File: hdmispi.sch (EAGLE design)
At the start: 3 parts

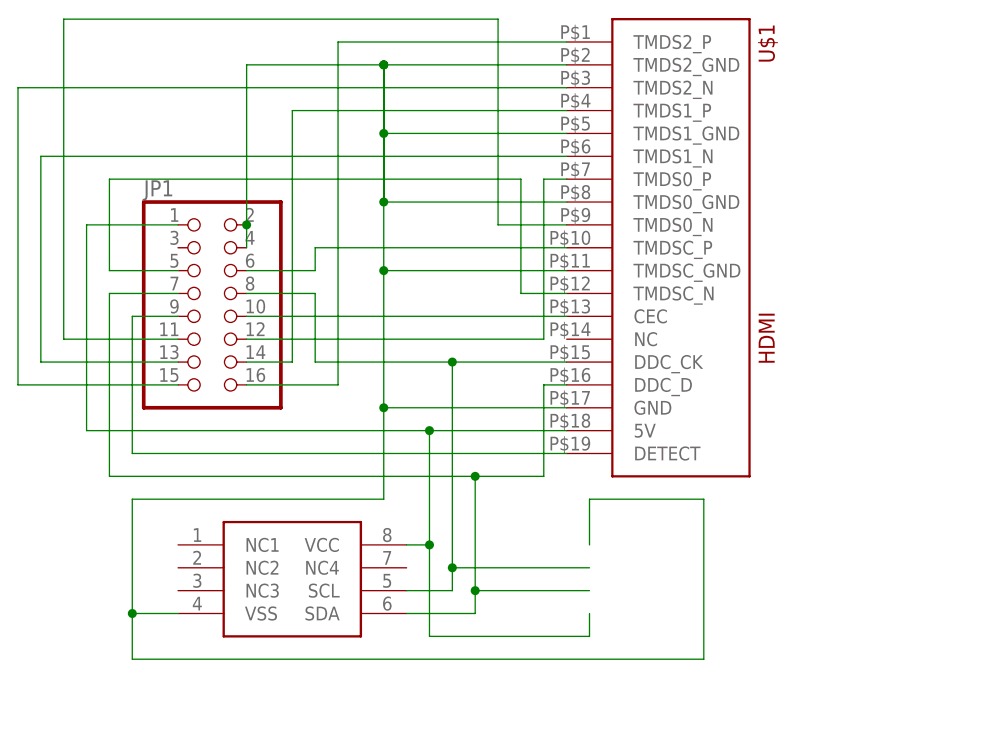
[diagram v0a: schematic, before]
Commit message: next rev of files, v1.0. Switched SDA/SCL wires by accident, doesn't work.
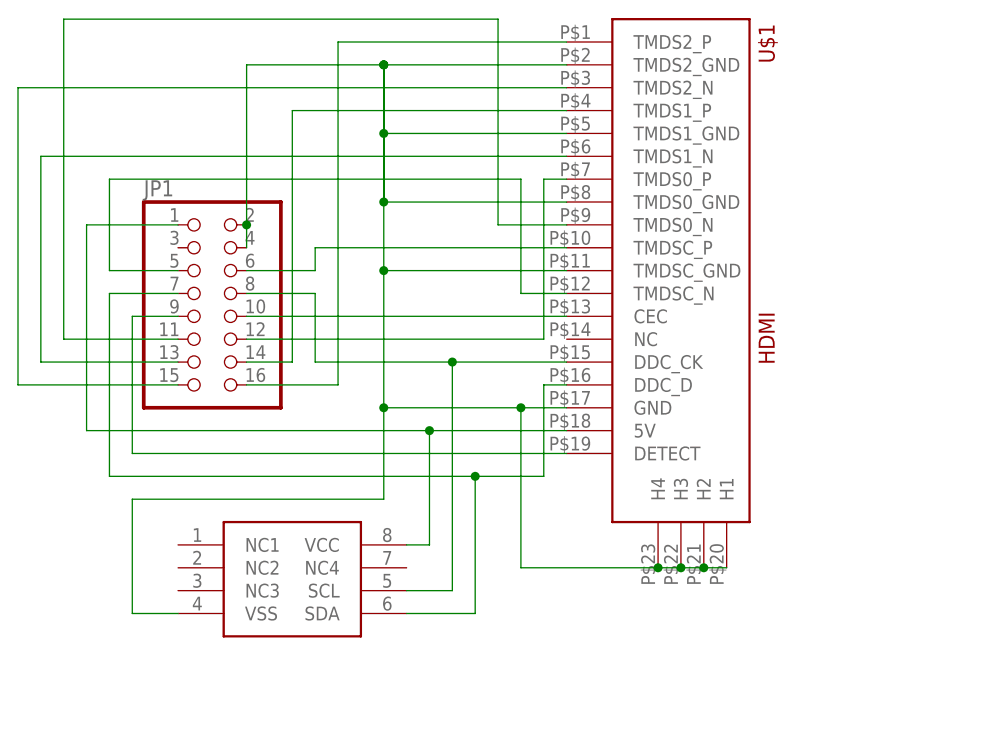
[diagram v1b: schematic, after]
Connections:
- net GND: now also U$1.H1, U$1.H2, U$1.H3, U$1.H4
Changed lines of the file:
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@@
 <wire x1="38.1" y1="83.82" x2="38.1" y2="96.52" width="0.1524" layer="91"/>
 <junction x="38.1" y="96.52"/>
-<wire x1="38.1" y1="83.82" x2="38.1" y2="73.66" width="0.1524" layer="91"/>
-<wire x1="38.1" y1="73.66" x2="55.88" y2="73.66" width="0.1524" layer="91"/>
-<wire x1="55.88" y1="73.66" x2="55.88" y2="76.2" width="0.1524" layer="91"/>
-<junction x="38.1" y="83.82"/>
 </segment>
 </net>
@@
 <pinref part="U$1" gate="G$1" pin="GND"/>
 <wire x1="33.02" y1="114.3" x2="33.02" y2="99.06" width="0.1524" layer="91"/>
-<wire x1="33.02" y1="99.06" x2="53.34" y2="99.06" width="0.1524" layer="91"/>
+<wire x1="33.02" y1="99.06" x2="48.26" y2="99.06" width="0.1524" layer="91"/>
 <junction x="33.02" y="129.54"/>
 <junction x="33.02" y="121.92"/>
@@
 <junction x="33.02" y="137.16"/>
 <pinref part="U$1" gate="G$1" pin="TMDSC_GND"/>
+<wire x1="48.26" y1="99.06" x2="53.34" y2="99.06" width="0.1524" layer="91"/>
 <wire x1="53.34" y1="114.3" x2="33.02" y2="114.3" width="0.1524" layer="91"/>
 <junction x="33.02" y="114.3"/>
@@
 <wire x1="33.02" y1="88.9" x2="33.02" y2="99.06" width="0.1524" layer="91"/>
 <junction x="33.02" y="99.06"/>
-<wire x1="55.88" y1="83.82" x2="55.88" y2="88.9" width="0.1524" layer="91"/>
-<wire x1="55.88" y1="88.9" x2="68.58" y2="88.9" width="0.1524" layer="91"/>
-<wire x1="68.58" y1="88.9" x2="68.58" y2="71.12" width="0.1524" layer="91"/>
-<wire x1="68.58" y1="71.12" x2="5.08" y2="71.12" width="0.1524" layer="91"/>
-<wire x1="5.08" y1="71.12" x2="5.08" y2="76.2" width="0.1524" layer="91"/>
-<junction x="5.08" y="76.2"/>
+<junction x="48.26" y="99.06"/>
+<wire x1="48.26" y1="99.06" x2="48.26" y2="81.28" width="0.1524" layer="91"/>
+<pinref part="U$1" gate="G$1" pin="H4"/>
+<junction x="63.5" y="81.28"/>
+<wire x1="48.26" y1="81.28" x2="63.5" y2="81.28" width="0.1524" layer="91"/>
+<pinref part="U$1" gate="G$1" pin="H3"/>
+<junction x="66.04" y="81.28"/>
+<wire x1="63.5" y1="81.28" x2="66.04" y2="81.28" width="0.1524" layer="91"/>
+<pinref part="U$1" gate="G$1" pin="H2"/>
+<junction x="68.58" y="81.28"/>
+<wire x1="66.04" y1="81.28" x2="68.58" y2="81.28" width="0.1524" layer="91"/>
+<pinref part="U$1" gate="G$1" pin="H1"/>
+<wire x1="68.58" y1="81.28" x2="71.12" y2="81.28" width="0.1524" layer="91"/>
 </segment>
 </net>
@@
 <pinref part="U$2" gate="G$1" pin="SDA"/>
 <wire x1="35.56" y1="76.2" x2="43.18" y2="76.2" width="0.1524" layer="91"/>
-<wire x1="43.18" y1="76.2" x2="43.18" y2="78.74" width="0.1524" layer="91"/>
 <junction x="43.18" y="91.44"/>
-<wire x1="43.18" y1="78.74" x2="43.18" y2="91.44" width="0.1524" layer="91"/>
-<wire x1="43.18" y1="78.74" x2="55.88" y2="78.74" width="0.1524" layer="91"/>
-<junction x="43.18" y="78.74"/>
+<wire x1="43.18" y1="76.2" x2="43.18" y2="91.44" width="0.1524" layer="91"/>
 </segment>
 </net>
@@
 <pinref part="U$2" gate="G$1" pin="SCL"/>
 <wire x1="35.56" y1="78.74" x2="40.64" y2="78.74" width="0.1524" layer="91"/>
-<wire x1="40.64" y1="78.74" x2="40.64" y2="81.28" width="0.1524" layer="91"/>
 <junction x="40.64" y="104.14"/>
-<wire x1="40.64" y1="81.28" x2="40.64" y2="104.14" width="0.1524" layer="91"/>
-<wire x1="40.64" y1="81.28" x2="55.88" y2="81.28" width="0.1524" layer="91"/>
-<junction x="40.64" y="81.28"/>
+<wire x1="40.64" y1="78.74" x2="40.64" y2="104.14" width="0.1524" layer="91"/>
 </segment>
 </net>

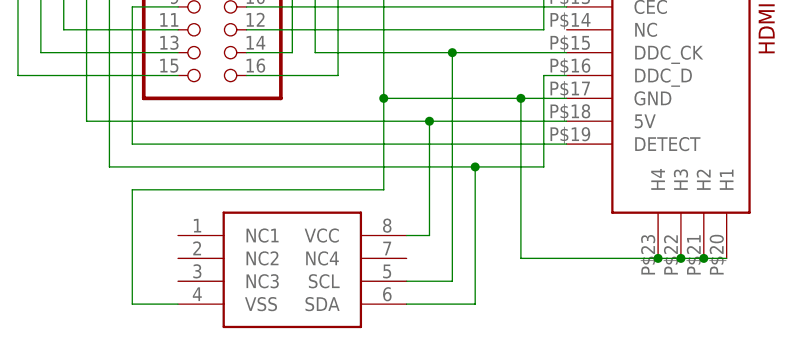
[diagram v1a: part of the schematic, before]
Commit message: fixed board and schematic with sda/scl corrected.
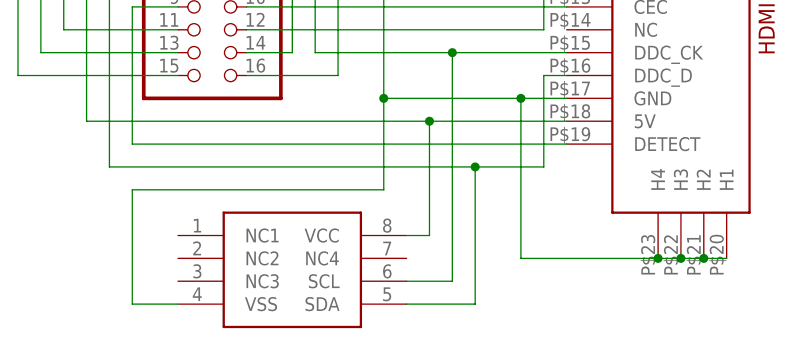
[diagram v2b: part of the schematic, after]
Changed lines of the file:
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@@
 <?xml version="1.0" encoding="utf-8"?>
 <!DOCTYPE eagle SYSTEM "eagle.dtd">
-<eagle version="7.2.0">
+<eagle version="7.6.0">
 <drawing>
 <settings>

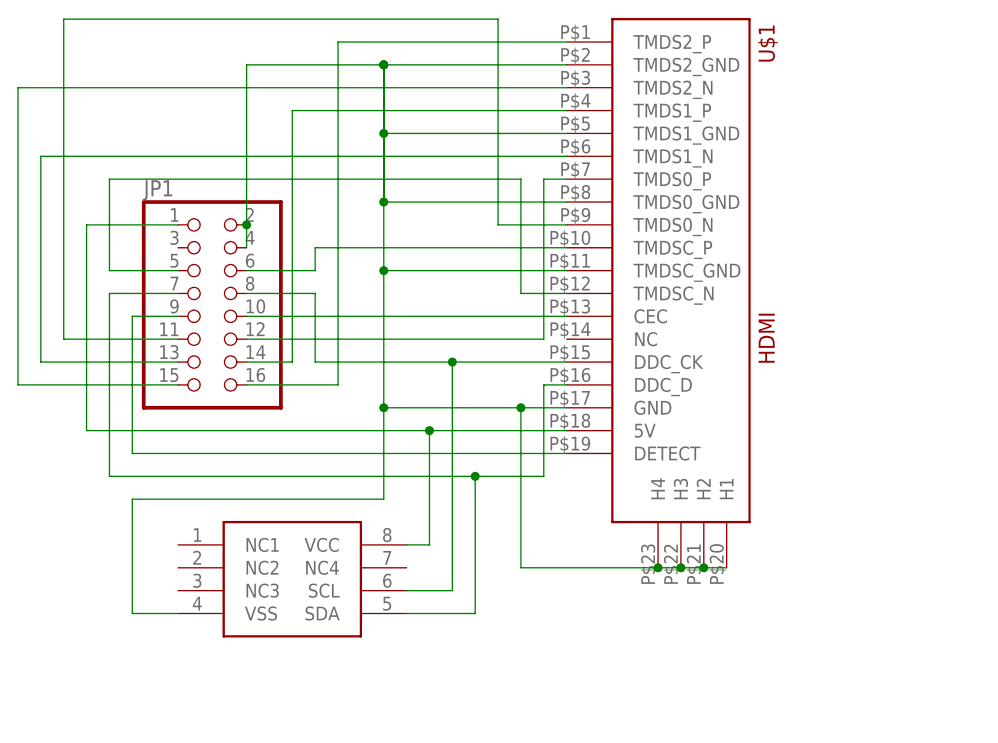
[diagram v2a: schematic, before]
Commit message: Modified to use a male hdmi splint connector that straddles the edge of the pcb. no longer a full breeakout, only the bare essentials for i2c work
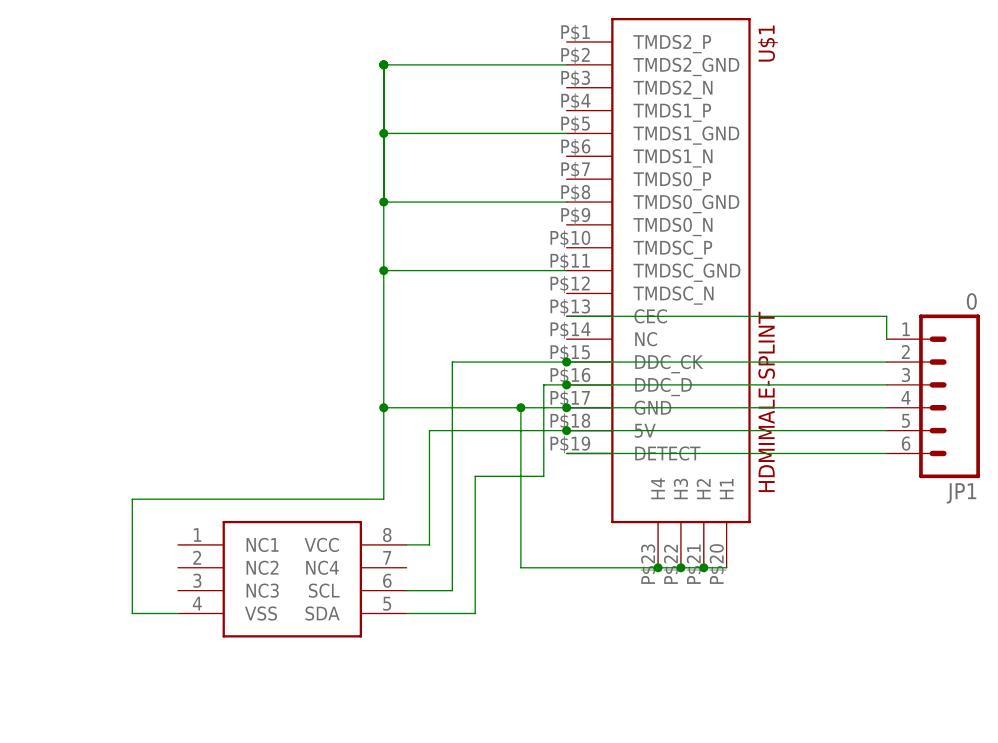
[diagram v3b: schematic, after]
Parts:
- JP1: value (none) -> 0; device pinhead:PINHD-2X8 -> SparkFun-Connectors:M06SIP_LOCK
- U$1: value HDMI -> HDMIMALE-SPLINT; device hdmispi:HDMI -> hdmispi:HDMIMALE-SPLINT
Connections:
- removed net CEC: JP1.10, U$1.CEC
- removed net DETECT: JP1.9, U$1.DETECT
- removed net TMDS0_N: JP1.11, U$1.TMDS0_N
- removed net TMDS0_P: JP1.12, U$1.TMDS0_P
- removed net TMDS1_N: JP1.13, U$1.TMDS1_N
- removed net TMDS1_P: JP1.14, U$1.TMDS1_P
- removed net TMDS2_N: JP1.15, U$1.TMDS2_N
- removed net TMDS2_P: JP1.16, U$1.TMDS2_P
- removed net TMDSC_N: JP1.5, U$1.TMDSC_N
- removed net TMDSC_P: JP1.6, U$1.TMDSC_P
- new net N$1: JP1.6, U$1.DETECT
- new net N$3: JP1.1, U$1.CEC
- net 5V: now also JP1.5; no longer JP1.1
- net DDC_CK: now also JP1.2; no longer JP1.8
- net DDC_D: now also JP1.3; no longer JP1.7
- net GND: no longer JP1.2
